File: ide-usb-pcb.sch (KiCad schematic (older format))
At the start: 4 parts, among them J1 STM32F4_Discovery_Header, J2 Conn_02x20_Odd_Even, U1 TXS0108EPW, U2 TXS0108EPW

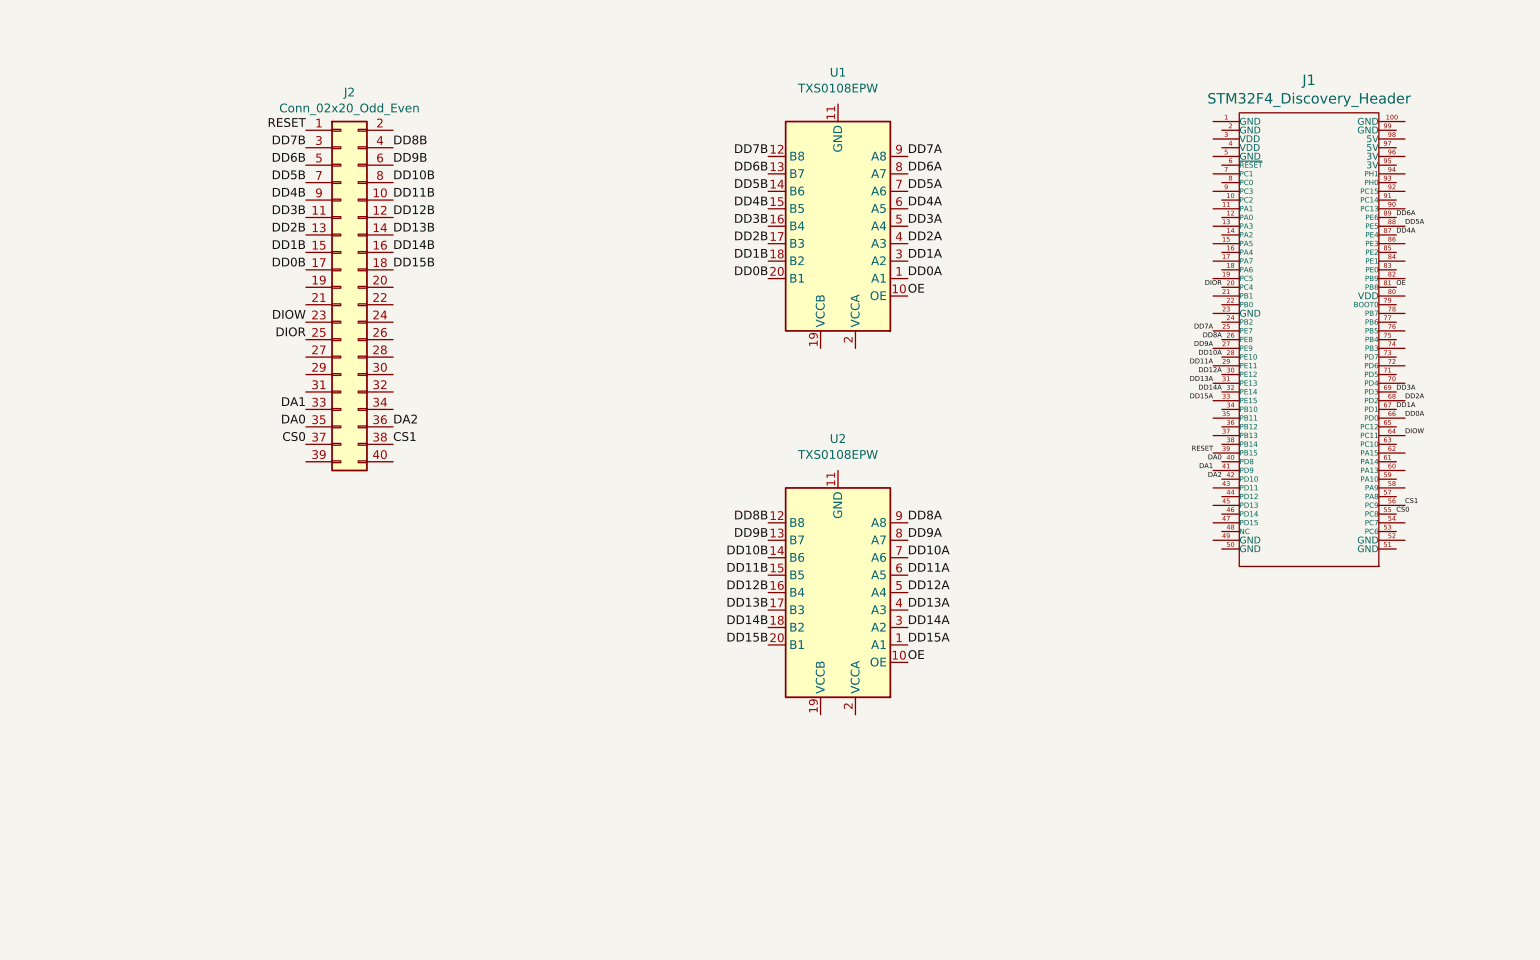
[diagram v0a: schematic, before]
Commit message: Add power & GND nets
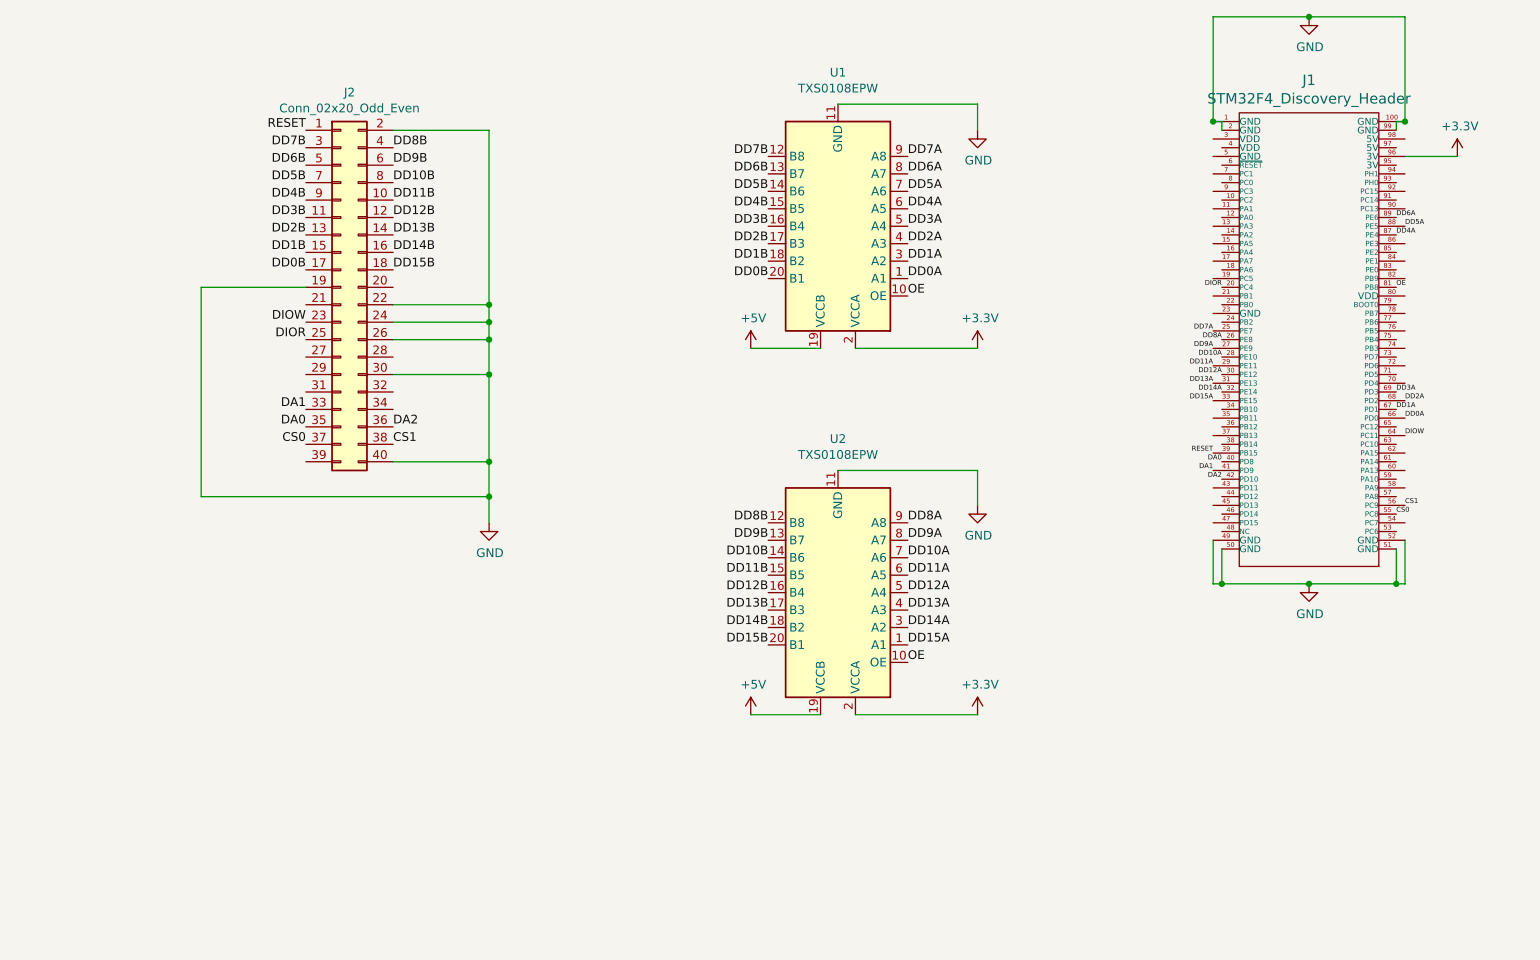
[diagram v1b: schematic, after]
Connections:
- net GND: now reaches U1.11 (GND)
- net GND: now also J1.1 (GND), J1.100 (GND), J1.2 (GND), J1.49 (GND), J1.50 (GND), J1.51 (GND), J1.52 (GND), J1.99 (GND), J2.19 (Pin_19), J2.2 (Pin_2), J2.22 (Pin_22), J2.24 (Pin_24), J2.26 (Pin_26), J2.30 (Pin_30), J2.40 (Pin_40), U2.11 (GND)
- net +5V: now reaches U1.19 (VCCB)
- net +5V: now also U2.19 (VCCB)
- net +3V3: now reaches U1.2 (VCCA)
- net +3V3: now also J1.96 (3V), U2.2 (VCCA)
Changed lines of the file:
@@
 Text Label 8750 3650 0    28   ~ 0
 CS1
+$Comp
+L power:GND #PWR?
+U 1 1 60E7BC45
+P 6300 1500
+F 0 "#PWR?" H 6300 1250 50  0001 C CNN
+F 1 "GND" H 6305 1327 50  0000 C CNN
+F 2 "" H 6300 1500 50  0001 C CNN
+F 3 "" H 6300 1500 50  0001 C CNN
+	1    6300 1500
+	1    0    0    -1
+$EndComp
+Wire Wire Line
+	5500 1350 6300 1350
+Wire Wire Line
+	6300 1350 6300 1500
+$Comp
+L power:GND #PWR?
+U 1 1 60E7F711
+P 6300 3650
+F 0 "#PWR?" H 6300 3400 50  0001 C CNN
+F 1 "GND" H 6305 3477 50  0000 C CNN
+F 2 "" H 6300 3650 50  0001 C CNN
+F 3 "" H 6300 3650 50  0001 C CNN
+	1    6300 3650
+	1    0    0    -1
+$EndComp
+Wire Wire Line
+	5500 3450 6300 3450
+Wire Wire Line
+	6300 3450 6300 3650
+$Comp
+L power:+5V #PWR?
+U 1 1 60E80DDE
+P 5000 2750
+F 0 "#PWR?" H 5000 2600 50  0001 C CNN
+F 1 "+5V" H 5015 2923 50  0000 C CNN
+F 2 "" H 5000 2750 50  0001 C CNN
+F 3 "" H 5000 2750 50  0001 C CNN
+	1    5000 2750
+	1    0    0    -1
+$EndComp
+Wire Wire Line
+	5400 2750 5000 2750
+$Comp
+L power:+5V #PWR?
+U 1 1 60E82DF1
+P 5000 4850
+F 0 "#PWR?" H 5000 4700 50  0001 C CNN
+F 1 "+5V" H 5015 5023 50  0000 C CNN
+F 2 "" H 5000 4850 50  0001 C CNN
+F 3 "" H 5000 4850 50  0001 C CNN
+	1    5000 4850
+	1    0    0    -1
+$EndComp
+Wire Wire Line
+	5400 4850 5000 4850
+$Comp
+L power:+3.3V #PWR?
+U 1 1 60E859BD
+P 6300 4850
+F 0 "#PWR?" H 6300 4700 50  0001 C CNN
+F 1 "+3.3V" H 6315 5023 50  0000 C CNN
+F 2 "" H 6300 4850 50  0001 C CNN
+F 3 "" H 6300 4850 50  0001 C CNN
+	1    6300 4850
+	1    0    0    -1
+$EndComp
+$Comp
+L power:+3.3V #PWR?
+U 1 1 60E85EE0
+P 6300 2750
+F 0 "#PWR?" H 6300 2600 50  0001 C CNN
+F 1 "+3.3V" H 6315 2923 50  0000 C CNN
+F 2 "" H 6300 2750 50  0001 C CNN
+F 3 "" H 6300 2750 50  0001 C CNN
+	1    6300 2750
+	1    0    0    -1
+$EndComp
+Wire Wire Line
+	6300 4850 5600 4850
+Wire Wire Line
+	6300 2750 5600 2750
+$Comp
+L power:+3.3V #PWR?
+U 1 1 60E8794A
+P 9050 1650
+F 0 "#PWR?" H 9050 1500 50  0001 C CNN
+F 1 "+3.3V" H 9065 1823 50  0000 C CNN
+F 2 "" H 9050 1650 50  0001 C CNN
+F 3 "" H 9050 1650 50  0001 C CNN
+	1    9050 1650
+	1    0    0    -1
+$EndComp
+Wire Wire Line
+	9050 1650 8750 1650
+$Comp
+L power:GND #PWR?
+U 1 1 60E88E46
+P 8200 4100
+F 0 "#PWR?" H 8200 3850 50  0001 C CNN
+F 1 "GND" H 8205 3927 50  0000 C CNN
+F 2 "" H 8200 4100 50  0001 C CNN
+F 3 "" H 8200 4100 50  0001 C CNN
+	1    8200 4100
+	1    0    0    -1
+$EndComp
+Wire Wire Line
+	7700 3900 7700 4100
+Wire Wire Line
+	7700 4100 8200 4100
+Wire Wire Line
+	8200 4100 8700 4100
+Wire Wire Line
+	8700 4100 8700 3900
+Connection ~ 8200 4100
+Wire Wire Line
+	7650 3850 7650 4100
+Wire Wire Line
+	7650 4100 7700 4100
+Connection ~ 7700 4100
+Wire Wire Line
+	8750 3850 8750 4100
+Wire Wire Line
+	8750 4100 8700 4100
+Connection ~ 8700 4100
+$Comp
+L power:GND #PWR?
+U 1 1 60E8B6E4
+P 8200 850
+F 0 "#PWR?" H 8200 600 50  0001 C CNN
+F 1 "GND" H 8205 677 50  0000 C CNN
+F 2 "" H 8200 850 50  0001 C CNN
+F 3 "" H 8200 850 50  0001 C CNN
+	1    8200 850
+	1    0    0    -1
+$EndComp
+Wire Wire Line
+	7650 1450 7650 850
+Wire Wire Line
+	7650 850  8200 850
+Wire Wire Line
+	8750 1450 8750 850
+Wire Wire Line
+	8750 850  8200 850
+Connection ~ 8200 850
+Wire Wire Line
+	7700 1500 7700 1450
+Wire Wire Line
+	7700 1450 7650 1450
+Connection ~ 7650 1450
+Wire Wire Line
+	8700 1500 8700 1450
+Wire Wire Line
+	8700 1450 8750 1450
+Connection ~ 8750 1450
+$Comp
+L power:GND #PWR?
+U 1 1 60E8F739
+P 3500 3750
+F 0 "#PWR?" H 3500 3500 50  0001 C CNN
+F 1 "GND" H 3505 3577 50  0000 C CNN
+F 2 "" H 3500 3750 50  0001 C CNN
+F 3 "" H 3500 3750 50  0001 C CNN
+	1    3500 3750
+	1    0    0    -1
+$EndComp
+Wire Wire Line
+	2950 3400 3500 3400
+Wire Wire Line
+	3500 3400 3500 3600
+Wire Wire Line
+	2950 2900 3500 2900
+Wire Wire Line
+	3500 2900 3500 3400
+Connection ~ 3500 3400
+Wire Wire Line
+	2950 2700 3500 2700
+Wire Wire Line
+	3500 2700 3500 2900
+Connection ~ 3500 2900
+Wire Wire Line
+	2950 2600 3500 2600
+Connection ~ 3500 2700
+Wire Wire Line
+	2950 2500 3500 2500
+Wire Wire Line
+	3500 2500 3500 2600
+Connection ~ 3500 2600
+Wire Wire Line
+	3500 2600 3500 2700
+Wire Wire Line
+	2950 1500 3500 1500
+Wire Wire Line
+	3500 1500 3500 2500
+Connection ~ 3500 2500
+Wire Wire Line
+	2450 2400 1850 2400
+Wire Wire Line
+	1850 2400 1850 3600
+Wire Wire Line
+	1850 3600 3500 3600
+Connection ~ 3500 3600
+Wire Wire Line
+	3500 3600 3500 3750
 $EndSCHEMATC

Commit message: Add termination resistors
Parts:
- added R1, R11, R12, R13, R14, R15, R16, R17, R18, R19, R2, R20, R21, R22, R23, R24, R3, R4, R5, R6, R7, R8: 33, Resistors_THT:R_Axial_DIN0204_L3.6mm_D1.6mm_P7.62mm_Horizontal, symbol Device:R
- added R10, R9: 22, Resistors_THT:R_Axial_DIN0204_L3.6mm_D1.6mm_P7.62mm_Horizontal, symbol Device:R
- renumbered J2 to J1, J1 to J2
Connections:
- net CS0: now also R13.2; no longer J1.37 (Pin_37)
- net CS1: now also R23.1; no longer J1.38 (Pin_38)
- net DA0: now also R12.2; no longer J1.35 (Pin_35)
- net DA1: now also R11.2; no longer J1.33 (Pin_33)
- net DA2: now also R22.1; no longer J1.36 (Pin_36)
- net DD0B: now also R8.2; no longer J1.17 (Pin_17)
- net DD10B: now also R16.1; no longer J1.8 (Pin_8)
- net DD11B: now also R17.1; no longer J1.10 (Pin_10)
- net DD12B: now also R18.1; no longer J1.12 (Pin_12)
- net DD13B: now also R19.1; no longer J1.14 (Pin_14)
- net DD14B: now also R20.1; no longer J1.16 (Pin_16)
- net DD15B: now also R21.1; no longer J1.18 (Pin_18)
- net DD1B: now also R7.2; no longer J1.15 (Pin_15)
- net DD2B: now also R6.2; no longer J1.13 (Pin_13)
- net DD3B: now also R5.2; no longer J1.11 (Pin_11)
- net DD4B: now also R4.2; no longer J1.9 (Pin_9)
- net DD5B: now also R3.2; no longer J1.7 (Pin_7)
- net DD6B: now also R2.2; no longer J1.5 (Pin_5)
- net DD7B: now also R1.2; no longer J1.3 (Pin_3)
- net DD8B: now also R14.1; no longer J1.4 (Pin_4)
- net DD9B: now also R15.1; no longer J1.6 (Pin_6)
- net DIOR: now also R10.2; no longer J1.25 (Pin_25)
- net DIOW: now also R9.2; no longer J1.23 (Pin_23)
- net RESET: now also R24.2; no longer J1.1 (Pin_1)
- new net: J1.1 (Pin_1), R24.1
- new net: J1.10 (Pin_10), R17.2
- new net: J1.11 (Pin_11), R5.1
- new net: J1.12 (Pin_12), R18.2
- new net: J1.13 (Pin_13), R6.1
- new net: J1.14 (Pin_14), R19.2
- new net: J1.15 (Pin_15), R7.1
- new net: J1.16 (Pin_16), R20.2
- new net: J1.17 (Pin_17), R8.1
- new net: J1.18 (Pin_18), R21.2
- new net: J1.23 (Pin_23), R9.1
- new net: J1.25 (Pin_25), R10.1
- new net: J1.3 (Pin_3), R1.1
- new net: J1.33 (Pin_33), R11.1
- new net: J1.35 (Pin_35), R12.1
- new net: J1.36 (Pin_36), R22.2
- new net: J1.37 (Pin_37), R13.1
- new net: J1.38 (Pin_38), R23.2
- new net: J1.4 (Pin_4), R14.2
- new net: J1.5 (Pin_5), R2.1
- new net: J1.6 (Pin_6), R15.2
- new net: J1.7 (Pin_7), R3.1
- new net: J1.8 (Pin_8), R16.2
- new net: J1.9 (Pin_9), R4.1

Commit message: Add power connectors
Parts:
- added J3: Screw_Terminal_01x02, TerminalBlocks_Phoenix:TerminalBlock_Phoenix_MPT-2.54mm_2pol, symbol Connector:Screw_Terminal_01x02
- added J4: USB_B, Connectors:USB_B, symbol Connector:USB_B
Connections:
- net +5V: now also J3.1 (Pin_1), J4.1 (VBUS)
- net GND: now also J3.2 (Pin_2), J4.4 (GND), J4.5 (Shield)
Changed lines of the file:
@@
 	0    1    1    0
 $EndComp
+$Comp
+L Connector:Screw_Terminal_01x02 J3
+U 1 1 60EB6BDB
+P 2650 4400
+F 0 "J3" H 2730 4392 50  0000 L CNN
+F 1 "Screw_Terminal_01x02" H 2730 4301 50  0000 L CNN
+F 2 "TerminalBlocks_Phoenix:TerminalBlock_Phoenix_MPT-2.54mm_2pol" H 2650 4400 50  0001 C CNN
+F 3 "~" H 2650 4400 50  0001 C CNN
+	1    2650 4400
+	1    0    0    -1
+$EndComp
+$Comp
+L power:GND #PWR012
+U 1 1 60EB9210
+P 2450 4500
+F 0 "#PWR012" H 2450 4250 50  0001 C CNN
+F 1 "GND" H 2455 4327 50  0000 C CNN
+F 2 "" H 2450 4500 50  0001 C CNN
+F 3 "" H 2450 4500 50  0001 C CNN
+	1    2450 4500
+	1    0    0    -1
+$EndComp
+$Comp
+L power:+5V #PWR011
+U 1 1 60EB9980
+P 2450 4400
+F 0 "#PWR011" H 2450 4250 50  0001 C CNN
+F 1 "+5V" H 2465 4573 50  0000 C CNN
+F 2 "" H 2450 4400 50  0001 C CNN
+F 3 "" H 2450 4400 50  0001 C CNN
+	1    2450 4400
+	1    0    0    -1
+$EndComp
+$Comp
+L Connector:USB_B J4
+U 1 1 60EC8A03
+P 2500 5400
+F 0 "J4" H 2557 5867 50  0000 C CNN
+F 1 "USB_B" H 2557 5776 50  0000 C CNN
+F 2 "Connectors:USB_B" H 2650 5350 50  0001 C CNN
+F 3 " ~" H 2650 5350 50  0001 C CNN
+	1    2500 5400
+	1    0    0    -1
+$EndComp
+$Comp
+L power:+5V #PWR014
+U 1 1 60EC9E44
+P 2800 5200
+F 0 "#PWR014" H 2800 5050 50  0001 C CNN
+F 1 "+5V" H 2815 5373 50  0000 C CNN
+F 2 "" H 2800 5200 50  0001 C CNN
+F 3 "" H 2800 5200 50  0001 C CNN
+	1    2800 5200
+	1    0    0    -1
+$EndComp
+$Comp
+L power:GND #PWR013
+U 1 1 60ECCE31
+P 2500 5950
+F 0 "#PWR013" H 2500 5700 50  0001 C CNN
+F 1 "GND" H 2505 5777 50  0000 C CNN
+F 2 "" H 2500 5950 50  0001 C CNN
+F 3 "" H 2500 5950 50  0001 C CNN
+	1    2500 5950
+	1    0    0    -1
+$EndComp
+Wire Wire Line
+	2500 5800 2500 5900
+Wire Wire Line
+	2400 5800 2400 5900
+Wire Wire Line
+	2400 5900 2500 5900
+Connection ~ 2500 5900
+Wire Wire Line
+	2500 5900 2500 5950
 $EndSCHEMATC

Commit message: First PCB version with everything routed
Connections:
- net DD10A: now also U2.4 (A3); no longer U2.7 (A6)
- net DD10B: now also U2.17 (B3); no longer U2.14 (B6)
- net DD11A: now also U2.5 (A4); no longer U2.6 (A5)
- net DD11B: now also U2.16 (B4); no longer U2.15 (B5)
- net DD12A: now also U2.6 (A5); no longer U2.5 (A4)
- net DD12B: now also U2.15 (B5); no longer U2.16 (B4)
- net DD13A: now also U2.7 (A6); no longer U2.4 (A3)
- net DD13B: now also U2.14 (B6); no longer U2.17 (B3)
- net DD14A: now also U2.8 (A7); no longer U2.3 (A2)
- net DD14B: now also U2.13 (B7); no longer U2.18 (B2)
- net DD15A: now also U2.9 (A8); no longer U2.1 (A1)
- net DD15B: now also U2.12 (B8); no longer U2.20 (B1)
- net DD8A: now also U2.1 (A1); no longer U2.9 (A8)
- net DD8B: now also U2.20 (B1); no longer U2.12 (B8)
- net DD9A: now also U2.3 (A2); no longer U2.8 (A7)
- net DD9B: now also U2.18 (B2); no longer U2.13 (B7)
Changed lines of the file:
@@
 Text Label 5100 2350 2    50   ~ 0
 DD0B
+Text Label 5100 4450 2    50   ~ 0
+DD8B
+Text Label 5100 4250 2    50   ~ 0
+DD10B
+Text Label 5100 4150 2    50   ~ 0
+DD11B
+Text Label 5100 4050 2    50   ~ 0
+DD12B
+Text Label 5100 3950 2    50   ~ 0
+DD13B
+Text Label 5100 3850 2    50   ~ 0
+DD14B
 Text Label 5100 3750 2    50   ~ 0
-DD8B
-Text Label 5100 3850 2    50   ~ 0
-DD9B
-Text Label 5100 3950 2    50   ~ 0
-DD10B
-Text Label 5100 4050 2    50   ~ 0
-DD11B
-Text Label 5100 4150 2    50   ~ 0
-DD12B
-Text Label 5100 4250 2    50   ~ 0
-DD13B
-Text Label 5100 4350 2    50   ~ 0
-DD14B
-Text Label 5100 4450 2    50   ~ 0
 DD15B
 Text Label 5900 1650 0    50   ~ 0
@@
 Text Label 5900 4550 0    50   ~ 0
 OE
+Text Label 5900 4450 0    50   ~ 0
+DD8A
+Text Label 5900 4350 0    50   ~ 0
+DD9A
+Text Label 5900 4250 0    50   ~ 0
+DD10A
+Text Label 5900 4150 0    50   ~ 0
+DD11A
+Text Label 5900 4050 0    50   ~ 0
+DD12A
+Text Label 5900 3950 0    50   ~ 0
+DD13A
+Text Label 5900 3850 0    50   ~ 0
+DD14A
 Text Label 5900 3750 0    50   ~ 0
-DD8A
-Text Label 5900 3850 0    50   ~ 0
-DD9A
-Text Label 5900 3950 0    50   ~ 0
-DD10A
-Text Label 5900 4050 0    50   ~ 0
-DD11A
-Text Label 5900 4150 0    50   ~ 0
-DD12A
-Text Label 5900 4250 0    50   ~ 0
-DD13A
-Text Label 5900 4350 0    50   ~ 0
-DD14A
-Text Label 5900 4450 0    50   ~ 0
 DD15A
 Text Label 8700 2400 0    28   ~ 0
@@
 Wire Wire Line
 	2500 5900 2500 5950
+Text Label 5100 4350 2    50   ~ 0
+DD9B
 $EndSCHEMATC

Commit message: Fix terminal block footprint
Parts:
- J3: footprint TerminalBlocks_Phoenix:TerminalBlock_Phoenix_MPT-2.54mm_2pol -> Connectors_Terminal_Blocks:TerminalBlock_bornier-2_P5.08mm
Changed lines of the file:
@@
 F 0 "J3" H 2730 4392 50  0000 L CNN
 F 1 "Screw_Terminal_01x02" H 2730 4301 50  0000 L CNN
-F 2 "TerminalBlocks_Phoenix:TerminalBlock_Phoenix_MPT-2.54mm_2pol" H 2650 4400 50  0001 C CNN
+F 2 "Connectors_Terminal_Blocks:TerminalBlock_bornier-2_P5.08mm" H 2650 4400 50  0001 C CNN
 F 3 "~" H 2650 4400 50  0001 C CNN
 	1    2650 4400

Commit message: Add OE pulldown resistor
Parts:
- added R25: 10K, Resistors_THT:R_Axial_DIN0204_L3.6mm_D1.6mm_P7.62mm_Horizontal, symbol Device:R
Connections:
- net GND: now also R25.2
- net OE: now also R25.1
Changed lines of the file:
@@
 Text Label 5100 4350 2    50   ~ 0
 DD9B
+$Comp
+L power:GND #PWR015
+U 1 1 60EA0A1D
+P 9200 2750
+F 0 "#PWR015" H 9200 2500 50  0001 C CNN
+F 1 "GND" H 9205 2577 50  0000 C CNN
+F 2 "" H 9200 2750 50  0001 C CNN
+F 3 "" H 9200 2750 50  0001 C CNN
+	1    9200 2750
+	1    0    0    -1
+$EndComp
+$Comp
+L Device:R R25
+U 1 1 60EA1456
+P 9200 2600
+F 0 "R25" H 9270 2646 50  0000 L CNN
+F 1 "10K" H 9270 2555 50  0000 L CNN
+F 2 "Resistors_THT:R_Axial_DIN0204_L3.6mm_D1.6mm_P7.62mm_Horizontal" V 9130 2600 50  0001 C CNN
+F 3 "~" H 9200 2600 50  0001 C CNN
+	1    9200 2600
+	1    0    0    -1
+$EndComp
+Wire Wire Line
+	8700 2400 9200 2400
+Wire Wire Line
+	9200 2400 9200 2450
 $EndSCHEMATC
